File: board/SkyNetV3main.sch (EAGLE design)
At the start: 66 parts, among them IC1 HC_05, IC2 RF4463PRO, IC3 LPC1769, IC4 BCX17, IC5 TPS63001, IC6 MCP73871-2CCI/ML, Q1 32.768KHz, Q2 12MHz, Q3 IRLM6402, Q4 BSS138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

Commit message: cleanup after routing
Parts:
- removed JP3: JTAG, microbuilder:HEADER-2X51.27MM
- removed JP4: EXT, skynet_other:PIN-HEAD-1X3
- removed X1: 52745-1290, con-molex:52745-1290
- added S3: (no value), sid:MOLEX-52892-1233
- added TP1, TP2: PTR1B1,27, testpad:PTR1B1,27
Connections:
- new net AD-EXT: IC3.P0[26]/AD0[3]/AOUT/RXD3, S3.11
- net +3V3: now also S3.1; no longer JP3.1, JP4.5
- net /BT-ON: now also IC3.P3[26]/STCLK/MAT0[1]/PWM1[3]; no longer IC3.P1[0]/ENET_TXD0
- net BT-AT: now also IC3.P0[25]/AD0[2]/I2SRX_SDA/TXD3; no longer IC3.P2[13]/EINT3/I2STX_SDA
- net BT-CN: now also IC3.P0[24]/AD0[1]/I2SRX_WS/CAP3[1]; no longer IC3.P0[10]/TXD2/SDA2/MAT3[0]
- net BT-RESET: now also IC3.P3[25]/MAT0[0]/PWM1[2]; no longer IC3.P0[11]/RXD2/SCL2/MAT3[1]
- net GND: now also S3.12, S3.CASE1, S3.CASE2; no longer JP3.3, JP3.5, JP3.9, JP4.6
- net JTAG_TCK: now also S3.10; no longer JP3.4
- net JTAG_TDI: now also S3.8; no longer JP3.8
- net JTAG_TDO: now also S3.7; no longer JP3.6
- net JTAG_TMS: now also S3.9; no longer JP3.2
- net LED-B: now also IC3.P1[18]/USB_UP_LED/PWM1[1]/CAP1[0]; no longer IC3.P2[0]/PWM1[1]/TXD1
- net LED-G: now also IC3.P1[21]/MCABORT/PWM1[3]/SSEL0; no longer IC3.P2[2]/PWM1[3]/CTS1/TRACEDATA[3]
- net LED-R: now also IC3.P1[20]/MCI0/PWM1[2]/SCK0; no longer IC3.P2[1]/PWM1[2]/RXD1
- net RESET: now also S3.4; no longer JP3.10
- net RX: now also S3.5, TP2.TP; no longer JP4.2
- net SCL-EXT: now also S3.3; no longer JP4.4
- net SDA-EXT: now also S3.2; no longer JP4.3
- net TX: now also S3.6, TP1.TP; no longer JP4.1
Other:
- note added: "Prog alternative"
- note removed: "JTAG"
- moved on the sheet: 1K, IC4, R1, R2, R4, R5, S1, S2, SJ2

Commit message: battery polarity revised
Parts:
- C6: device rcl:C-EUC1206K -> rcl:C-EUC0805
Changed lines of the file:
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@@
 <part name="R9" library="rcl" deviceset="R-EU_" device="R0603" value="10k"/>
 <part name="P+10" library="supply1" deviceset="+5V" device=""/>
-<part name="C6" library="rcl" deviceset="C-EU" device="C1206K" value="10u"/>
 <part name="GND23" library="supply1" deviceset="GND" device=""/>
 <part name="BAT+4" library="supply1" deviceset="V+" device=""/>
@@
 <part name="TP2" library="testpad" deviceset="PTR1" device="B1,27"/>
 <part name="+3V3" library="supply1" deviceset="+3V3" device=""/>
+<part name="C6" library="rcl" deviceset="C-EU" device="C0805" value="10u"/>
 </parts>
 <sheets>
@@
 <instance part="R9" gate="G$1" x="91.44" y="124.46" rot="R270"/>
 <instance part="P+10" gate="1" x="35.56" y="167.64"/>
-<instance part="C6" gate="G$1" x="35.56" y="127"/>
 <instance part="GND23" gate="1" x="35.56" y="106.68"/>
 <instance part="BAT+4" gate="1" x="114.3" y="165.1"/>
@@
 <instance part="IC5" gate="TH" x="48.26" y="27.94"/>
 <instance part="GND8" gate="1" x="43.18" y="22.86"/>
+<instance part="C6" gate="G$1" x="35.56" y="127"/>
 </instances>
 <busses>
@@
 <segment>
 <pinref part="GND23" gate="1" pin="GND"/>
+<wire x1="35.56" y1="109.22" x2="35.56" y2="121.92" width="0.1524" layer="91"/>
 <pinref part="C6" gate="G$1" pin="2"/>
-<wire x1="35.56" y1="109.22" x2="35.56" y2="121.92" width="0.1524" layer="91"/>
 </segment>
 <segment>
@@
 </segment>
 <segment>
-<pinref part="C6" gate="G$1" pin="1"/>
 <pinref part="P+10" gate="1" pin="+5V"/>
 <wire x1="35.56" y1="129.54" x2="35.56" y2="165.1" width="0.1524" layer="91"/>
-</segment>
-<segment>
+<pinref part="C6" gate="G$1" pin="1"/>
+</segment>
+<segment>

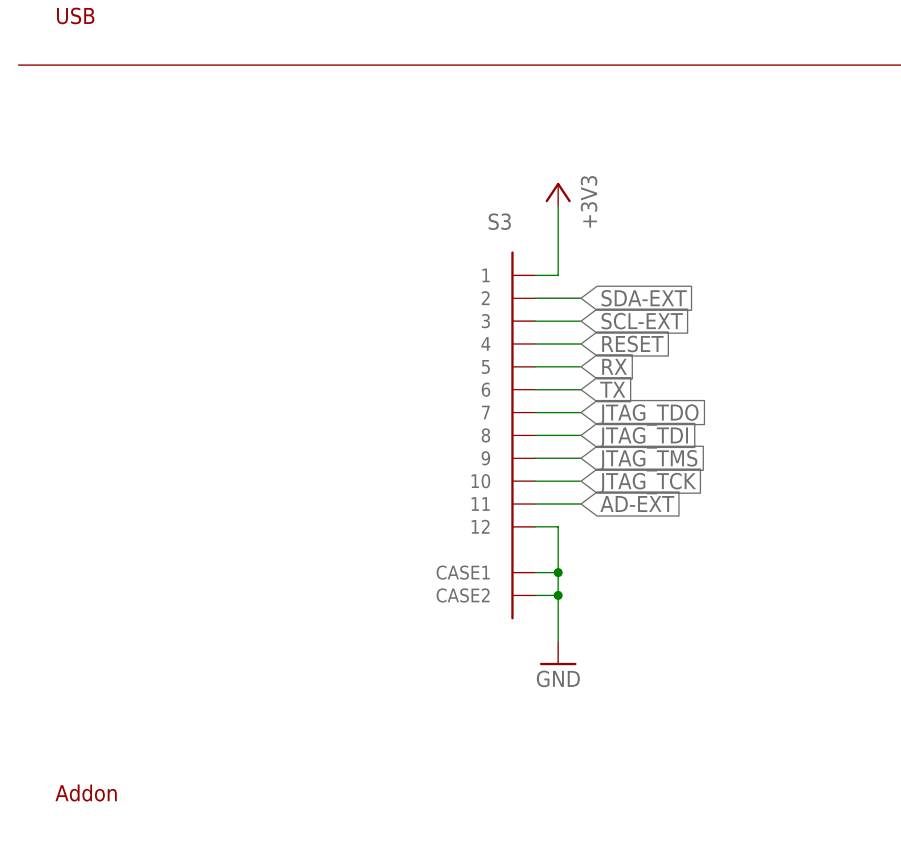
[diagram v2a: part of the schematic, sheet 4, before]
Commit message: new connector
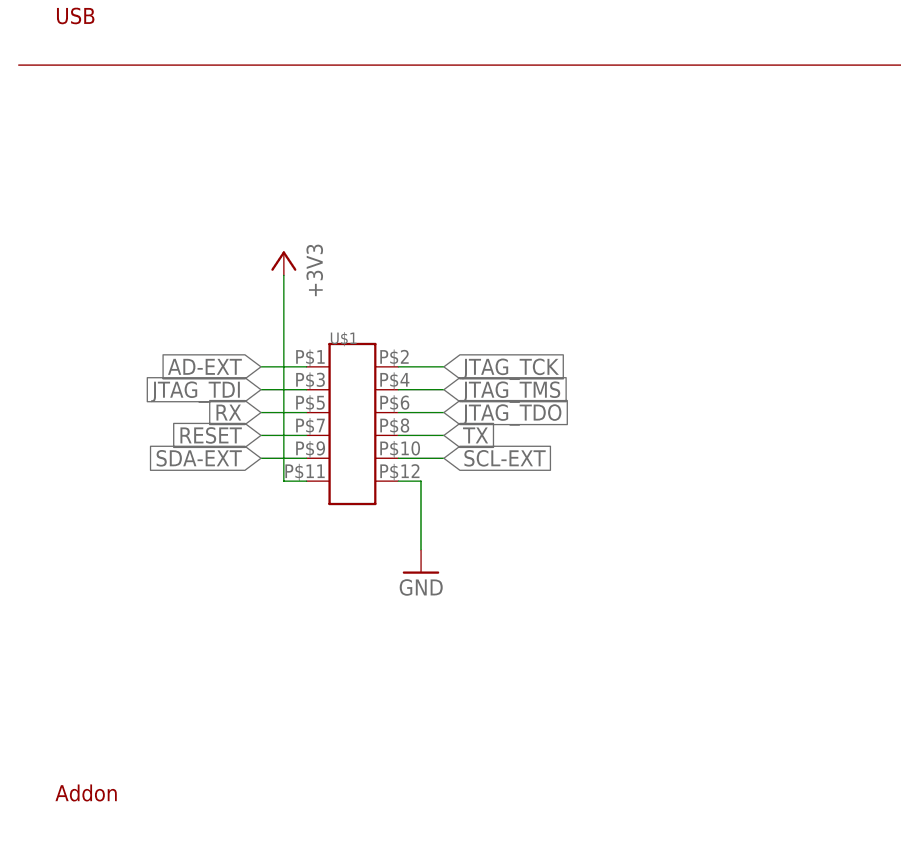
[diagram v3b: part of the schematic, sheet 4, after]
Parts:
- removed S3: (no value), sid:MOLEX-52892-1233
- added U$1: 2X6SMD2.0, i7:2X6SMD2.0
- renumbered 1K to R20
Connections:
- net +3V3: now also U$1.P$11; no longer S3.1
- net AD-EXT: now also U$1.P$1; no longer S3.11
- net GND: now also U$1.P$12; no longer S3.12, S3.CASE1, S3.CASE2
- net JTAG_TCK: now also U$1.P$2; no longer S3.10
- net JTAG_TDI: now also U$1.P$3; no longer S3.8
- net JTAG_TDO: now also U$1.P$6; no longer S3.7
- net JTAG_TMS: now also U$1.P$4; no longer S3.9
- net RESET: now also U$1.P$7; no longer S3.4
- net RX: now also U$1.P$5; no longer S3.5
- net SCL-EXT: now also U$1.P$10; no longer S3.3
- net SDA-EXT: now also U$1.P$9; no longer S3.2
- net TX: now also U$1.P$8; no longer S3.6
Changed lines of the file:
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@@
 <part name="+3V5" library="supply1" deviceset="+3V3" device=""/>
 <part name="IC4" library="skynet_other" deviceset="BCX17" device=""/>
-<part name="1K" library="rcl" deviceset="R-EU_" device="R0603" value="330"/>
+<part name="R20" library="rcl" deviceset="R-EU_" device="R0603" value="330"/>
 <part name="+3V9" library="supply1" deviceset="+3V3" device=""/>
 <part name="R4" library="rcl" deviceset="R-EU_" device="R0603" value="1k5"/>
@@
 <part name="B1" library="i7" deviceset="1S" device="" value="PL503465"/>
 <part name="GND8" library="supply1" deviceset="GND" device=""/>
-<part name="S3" library="sid" deviceset="MOLEX-52892-1233" device=""/>
 <part name="GND42" library="supply1" deviceset="GND" device=""/>
 <part name="TP1" library="testpad" deviceset="PTR1" device="B1,27"/>
@@
 <part name="+3V3" library="supply1" deviceset="+3V3" device=""/>
 <part name="C6" library="rcl" deviceset="C-EU" device="C0805" value="10u"/>
+<part name="U$1" library="i7" deviceset="2X6SMD2.0" device=""/>
 </parts>
 <sheets>
@@
 <instance part="+3V5" gate="G$1" x="215.9" y="172.72"/>
 <instance part="IC4" gate="G$1" x="195.58" y="119.38"/>
-<instance part="1K" gate="G$1" x="187.96" y="106.68" rot="R90"/>
+<instance part="R20" gate="G$1" x="187.96" y="106.68" rot="R90"/>
 <instance part="+3V9" gate="G$1" x="198.12" y="172.72"/>
 <instance part="R4" gate="G$1" x="198.12" y="106.68" rot="R90"/>
@@
 <pinref part="IC3" gate="G$1" pin="P2[9]/USB_CONNECT/RXD2/ENET_MDIO"/>
 <wire x1="160.02" y1="78.74" x2="187.96" y2="78.74" width="0.1524" layer="91"/>
-<pinref part="1K" gate="G$1" pin="1"/>
+<pinref part="R20" gate="G$1" pin="1"/>
 <wire x1="187.96" y1="78.74" x2="187.96" y2="101.6" width="0.1524" layer="91"/>
 </segment>
@@
 <net name="USB-CON-TRANS" class="0">
 <segment>
-<pinref part="1K" gate="G$1" pin="2"/>
+<pinref part="R20" gate="G$1" pin="2"/>
 <wire x1="187.96" y1="111.76" x2="187.96" y2="119.38" width="0.1524" layer="91"/>
 <pinref part="IC4" gate="G$1" pin="B"/>
@@
 <instance part="GND40" gate="1" x="68.58" y="114.3"/>
 <instance part="GND41" gate="1" x="78.74" y="114.3"/>
-<instance part="S3" gate="G$1" x="58.42" y="50.8" rot="MR0"/>
-<instance part="GND42" gate="1" x="63.5" y="22.86" rot="MR0"/>
+<instance part="GND42" gate="1" x="48.26" y="33.02" rot="MR0"/>
 <instance part="TP1" gate="G$1" x="195.58" y="58.42" rot="R270"/>
 <instance part="TP2" gate="G$1" x="195.58" y="53.34" rot="R270"/>
-<instance part="+3V3" gate="G$1" x="63.5" y="76.2" rot="MR0"/>
+<instance part="+3V3" gate="G$1" x="33.02" y="68.58" rot="MR0"/>
+<instance part="U$1" gate="G$1" x="40.64" y="48.26"/>
 </instances>
 <busses>
@@
 </segment>
 <segment>
-<pinref part="S3" gate="G$1" pin="CASE2"/>
+<pinref part="U$1" gate="G$1" pin="P$12"/>
 <pinref part="GND42" gate="1" pin="GND"/>
-<wire x1="60.96" y1="30.48" x2="63.5" y2="30.48" width="0.1524" layer="91"/>
-<wire x1="63.5" y1="30.48" x2="63.5" y2="25.4" width="0.1524" layer="91"/>
-<pinref part="S3" gate="G$1" pin="CASE1"/>
-<wire x1="60.96" y1="33.02" x2="63.5" y2="33.02" width="0.1524" layer="91"/>
-<wire x1="63.5" y1="33.02" x2="63.5" y2="30.48" width="0.1524" layer="91"/>
-<junction x="63.5" y="30.48"/>
-<pinref part="S3" gate="G$1" pin="12"/>
-<wire x1="60.96" y1="38.1" x2="63.5" y2="38.1" width="0.1524" layer="91"/>
-<wire x1="63.5" y1="38.1" x2="63.5" y2="33.02" width="0.1524" layer="91"/>
-<junction x="63.5" y="33.02"/>
+<wire x1="45.72" y1="43.18" x2="48.26" y2="43.18" width="0.1524" layer="91"/>
+<wire x1="48.26" y1="43.18" x2="48.26" y2="35.56" width="0.1524" layer="91"/>
 </segment>
 </net>
@@
 </segment>
 <segment>
-<pinref part="S3" gate="G$1" pin="1"/>
+<pinref part="U$1" gate="G$1" pin="P$11"/>
 <pinref part="+3V3" gate="G$1" pin="+3V3"/>
-<wire x1="60.96" y1="66.04" x2="63.5" y2="66.04" width="0.1524" layer="91"/>
-<wire x1="63.5" y1="66.04" x2="63.5" y2="73.66" width="0.1524" layer="91"/>
+<wire x1="35.56" y1="43.18" x2="33.02" y2="43.18" width="0.1524" layer="91"/>
+<wire x1="33.02" y1="43.18" x2="33.02" y2="66.04" width="0.1524" layer="91"/>
 </segment>
 </net>
@@
 <net name="SDA-EXT" class="0">
 <segment>
-<pinref part="S3" gate="G$1" pin="2"/>
-<wire x1="60.96" y1="63.5" x2="66.04" y2="63.5" width="0.1524" layer="91"/>
-<label x="66.04" y="63.5" size="1.778" layer="95" rot="MR180" xref="yes"/>
+<wire x1="35.56" y1="45.72" x2="30.48" y2="45.72" width="0.1524" layer="91"/>
+<label x="30.48" y="45.72" size="1.778" layer="95" rot="MR0" xref="yes"/>
+<pinref part="U$1" gate="G$1" pin="P$9"/>
 </segment>
 </net>
 <net name="SCL-EXT" class="0">
 <segment>
-<pinref part="S3" gate="G$1" pin="3"/>
-<wire x1="60.96" y1="60.96" x2="66.04" y2="60.96" width="0.1524" layer="91"/>
-<label x="66.04" y="60.96" size="1.778" layer="95" rot="MR180" xref="yes"/>
+<wire x1="45.72" y1="45.72" x2="50.8" y2="45.72" width="0.1524" layer="91"/>
+<label x="50.8" y="45.72" size="1.778" layer="95" rot="MR180" xref="yes"/>
+<pinref part="U$1" gate="G$1" pin="P$10"/>
 </segment>
 </net>
 <net name="RESET" class="0">
 <segment>
-<pinref part="S3" gate="G$1" pin="4"/>
-<wire x1="60.96" y1="58.42" x2="66.04" y2="58.42" width="0.1524" layer="91"/>
-<label x="66.04" y="58.42" size="1.778" layer="95" rot="MR180" xref="yes"/>
+<wire x1="35.56" y1="48.26" x2="30.48" y2="48.26" width="0.1524" layer="91"/>
+<label x="30.48" y="48.26" size="1.778" layer="95" rot="MR0" xref="yes"/>
+<pinref part="U$1" gate="G$1" pin="P$7"/>
 </segment>
 </net>
 <net name="JTAG_TMS" class="0">
 <segment>
-<pinref part="S3" gate="G$1" pin="9"/>
-<wire x1="60.96" y1="45.72" x2="66.04" y2="45.72" width="0.1524" layer="91"/>
-<label x="66.04" y="45.72" size="1.778" layer="95" rot="MR180" xref="yes"/>
+<wire x1="45.72" y1="53.34" x2="50.8" y2="53.34" width="0.1524" layer="91"/>
+<label x="50.8" y="53.34" size="1.778" layer="95" rot="MR180" xref="yes"/>
+<pinref part="U$1" gate="G$1" pin="P$4"/>
 </segment>
 </net>
 <net name="JTAG_TDO" class="0">
 <segment>
-<pinref part="S3" gate="G$1" pin="7"/>
-<wire x1="60.96" y1="50.8" x2="66.04" y2="50.8" width="0.1524" layer="91"/>
-<label x="66.04" y="50.8" size="1.778" layer="95" rot="MR180" xref="yes"/>
+<wire x1="45.72" y1="50.8" x2="50.8" y2="50.8" width="0.1524" layer="91"/>
+<label x="50.8" y="50.8" size="1.778" layer="95" rot="MR180" xref="yes"/>
+<pinref part="U$1" gate="G$1" pin="P$6"/>
 </segment>
 </net>
 <net name="JTAG_TDI" class="0">
 <segment>
-<pinref part="S3" gate="G$1" pin="8"/>
-<wire x1="60.96" y1="48.26" x2="66.04" y2="48.26" width="0.1524" layer="91"/>
-<label x="66.04" y="48.26" size="1.778" layer="95" rot="MR180" xref="yes"/>
+<wire x1="35.56" y1="53.34" x2="30.48" y2="53.34" width="0.1524" layer="91"/>
+<label x="30.48" y="53.34" size="1.778" layer="95" rot="MR0" xref="yes"/>
+<pinref part="U$1" gate="G$1" pin="P$3"/>
 </segment>
 </net>
 <net name="JTAG_TCK" class="0">
 <segment>
-<pinref part="S3" gate="G$1" pin="10"/>
-<wire x1="60.96" y1="43.18" x2="66.04" y2="43.18" width="0.1524" layer="91"/>
-<label x="66.04" y="43.18" size="1.778" layer="95" rot="MR180" xref="yes"/>
+<wire x1="45.72" y1="55.88" x2="50.8" y2="55.88" width="0.1524" layer="91"/>
+<label x="50.8" y="55.88" size="1.778" layer="95" rot="MR180" xref="yes"/>
+<pinref part="U$1" gate="G$1" pin="P$2"/>
 </segment>
 </net>
@@
 <net name="TX" class="0">
 <segment>
-<pinref part="S3" gate="G$1" pin="6"/>
-<wire x1="60.96" y1="53.34" x2="66.04" y2="53.34" width="0.1524" layer="91"/>
-<label x="66.04" y="53.34" size="1.778" layer="95" rot="MR180" xref="yes"/>
+<wire x1="45.72" y1="48.26" x2="50.8" y2="48.26" width="0.1524" layer="91"/>
+<label x="50.8" y="48.26" size="1.778" layer="95" rot="MR180" xref="yes"/>
+<pinref part="U$1" gate="G$1" pin="P$8"/>
 </segment>
 <segment>
@@
 <net name="RX" class="0">
 <segment>
-<pinref part="S3" gate="G$1" pin="5"/>
-<wire x1="60.96" y1="55.88" x2="66.04" y2="55.88" width="0.1524" layer="91"/>
-<label x="66.04" y="55.88" size="1.778" layer="95" rot="MR180" xref="yes"/>
+<wire x1="35.56" y1="50.8" x2="30.48" y2="50.8" width="0.1524" layer="91"/>
+<label x="30.48" y="50.8" size="1.778" layer="95" rot="MR0" xref="yes"/>
+<pinref part="U$1" gate="G$1" pin="P$5"/>
 </segment>
 <segment>
@@
 <net name="AD-EXT" class="0">
 <segment>
-<pinref part="S3" gate="G$1" pin="11"/>
-<wire x1="60.96" y1="40.64" x2="66.04" y2="40.64" width="0.1524" layer="91"/>
-<label x="66.04" y="40.64" size="1.778" layer="95" rot="MR180" xref="yes"/>
-</segment>
-</net>
+<wire x1="35.56" y1="55.88" x2="30.48" y2="55.88" width="0.1524" layer="91"/>
+<label x="30.48" y="55.88" size="1.778" layer="95" rot="MR0" xref="yes"/>
+<pinref part="U$1" gate="G$1" pin="P$1"/>
+</segment>
+</net>

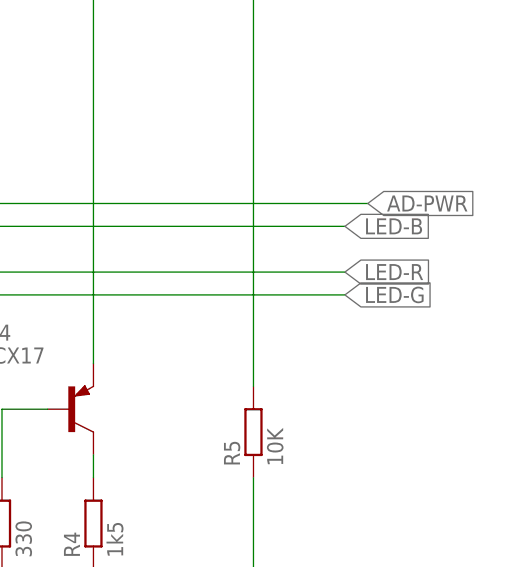
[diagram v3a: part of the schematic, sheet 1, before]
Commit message: net names corrected for led
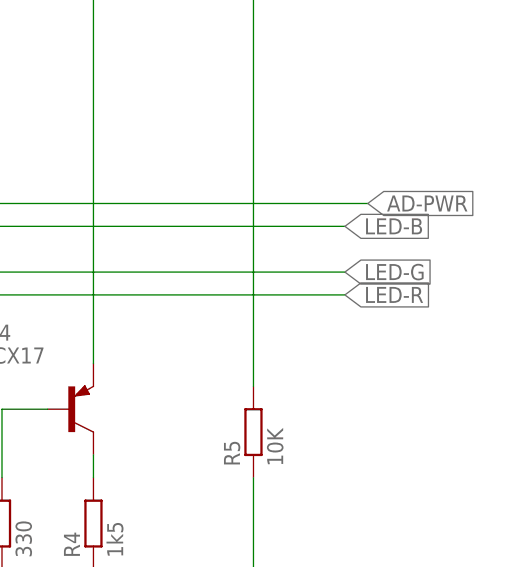
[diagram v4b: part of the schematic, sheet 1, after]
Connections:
- net LED-G: now also IC3.P1[20]/MCI0/PWM1[2]/SCK0; no longer IC3.P1[21]/MCABORT/PWM1[3]/SSEL0
- net LED-R: now also IC3.P1[21]/MCABORT/PWM1[3]/SSEL0; no longer IC3.P1[20]/MCI0/PWM1[2]/SCK0
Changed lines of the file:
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@@
 <?xml version="1.0" encoding="utf-8"?>
 <!DOCTYPE eagle SYSTEM "eagle.dtd">
-<eagle version="7.1.0">
+<eagle version="6.5.0">
 <drawing>
 <settings>
@@
 </segment>
 </net>
-<net name="LED-R" class="0">
-<segment>
-<pinref part="IC3" gate="G$1" pin="P1[20]/MCI0/PWM1[2]/SCK0"/>
-<wire x1="160.02" y1="134.62" x2="226.06" y2="134.62" width="0.1524" layer="91"/>
-<label x="226.06" y="134.62" size="1.778" layer="95" xref="yes"/>
-</segment>
-</net>
 <net name="INPUT" class="0">
 <segment>
@@
 <net name="LED-G" class="0">
 <segment>
-<pinref part="IC3" gate="G$1" pin="P1[21]/MCABORT/PWM1[3]/SSEL0"/>
-<wire x1="160.02" y1="132.08" x2="226.06" y2="132.08" width="0.1524" layer="91"/>
-<label x="226.06" y="132.08" size="1.778" layer="95" xref="yes"/>
+<pinref part="IC3" gate="G$1" pin="P1[20]/MCI0/PWM1[2]/SCK0"/>
+<wire x1="160.02" y1="134.62" x2="226.06" y2="134.62" width="0.1524" layer="91"/>
+<label x="226.06" y="134.62" size="1.778" layer="95" xref="yes"/>
 </segment>
 </net>
@@
 </segment>
 </net>
+<net name="LED-R" class="0">
+<segment>
+<pinref part="IC3" gate="G$1" pin="P1[21]/MCABORT/PWM1[3]/SSEL0"/>
+<wire x1="160.02" y1="132.08" x2="226.06" y2="132.08" width="0.1524" layer="91"/>
+<label x="226.06" y="132.08" size="1.778" layer="95" xref="yes"/>
+</segment>
+</net>

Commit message: Revert "net names corrected for led"
This reverts commit bfdfdada0646938294157fc6761012cd3f7e2628.

nets got damaged by renaming, better just adopt firmware instead
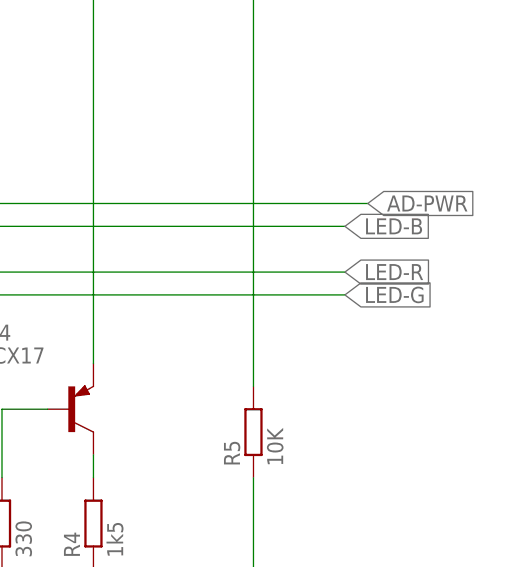
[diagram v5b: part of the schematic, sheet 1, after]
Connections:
- net LED-G: now also IC3.P1[21]/MCABORT/PWM1[3]/SSEL0; no longer IC3.P1[20]/MCI0/PWM1[2]/SCK0
- net LED-R: now also IC3.P1[20]/MCI0/PWM1[2]/SCK0; no longer IC3.P1[21]/MCABORT/PWM1[3]/SSEL0
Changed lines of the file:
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@@
 <?xml version="1.0" encoding="utf-8"?>
 <!DOCTYPE eagle SYSTEM "eagle.dtd">
-<eagle version="6.5.0">
+<eagle version="7.1.0">
 <drawing>
 <settings>
@@
 </segment>
 </net>
+<net name="LED-R" class="0">
+<segment>
+<pinref part="IC3" gate="G$1" pin="P1[20]/MCI0/PWM1[2]/SCK0"/>
+<wire x1="160.02" y1="134.62" x2="226.06" y2="134.62" width="0.1524" layer="91"/>
+<label x="226.06" y="134.62" size="1.778" layer="95" xref="yes"/>
+</segment>
+</net>
 <net name="INPUT" class="0">
 <segment>
@@
 <net name="LED-G" class="0">
 <segment>
-<pinref part="IC3" gate="G$1" pin="P1[20]/MCI0/PWM1[2]/SCK0"/>
-<wire x1="160.02" y1="134.62" x2="226.06" y2="134.62" width="0.1524" layer="91"/>
-<label x="226.06" y="134.62" size="1.778" layer="95" xref="yes"/>
+<pinref part="IC3" gate="G$1" pin="P1[21]/MCABORT/PWM1[3]/SSEL0"/>
+<wire x1="160.02" y1="132.08" x2="226.06" y2="132.08" width="0.1524" layer="91"/>
+<label x="226.06" y="132.08" size="1.778" layer="95" xref="yes"/>
 </segment>
 </net>
@@
 </segment>
 </net>
-<net name="LED-R" class="0">
-<segment>
-<pinref part="IC3" gate="G$1" pin="P1[21]/MCABORT/PWM1[3]/SSEL0"/>
-<wire x1="160.02" y1="132.08" x2="226.06" y2="132.08" width="0.1524" layer="91"/>
-<label x="226.06" y="132.08" size="1.778" layer="95" xref="yes"/>
-</segment>
-</net>
